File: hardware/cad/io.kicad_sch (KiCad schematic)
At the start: 29 parts, among them J1 DC POWER JACK, J2 1/4" JACK, STEREO, J23 2P_HEADER, J24 2P_HEADER, J25 2P_HEADER, J26 2P_HEADER, J3 6-440054-2, J4 6-440129-2, J5 1/4" JACK, STEREO

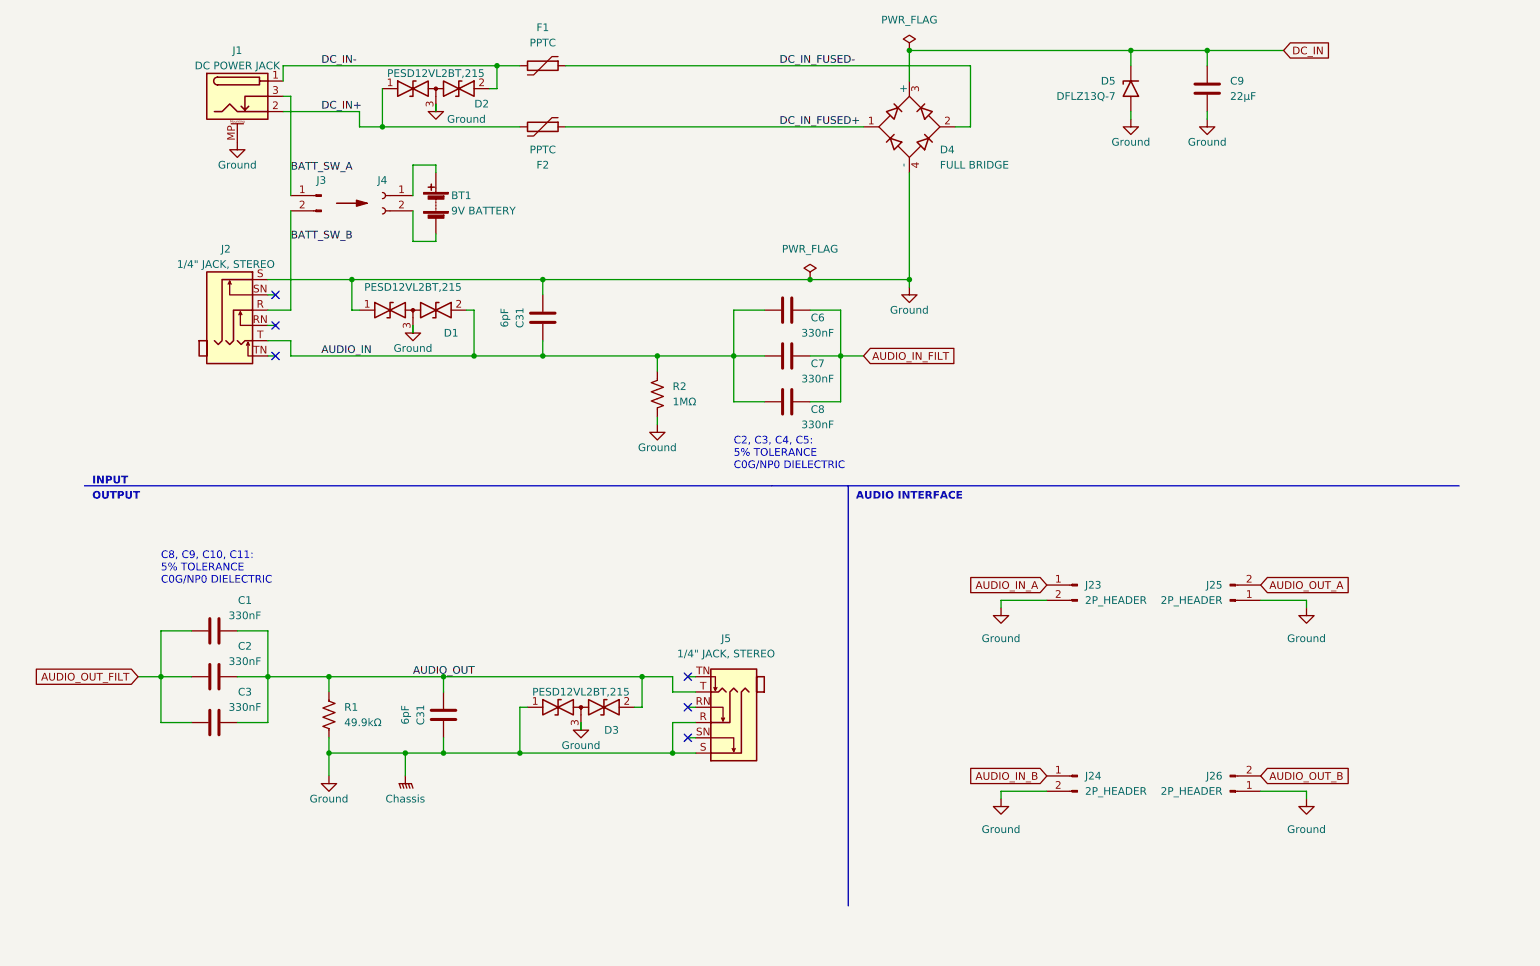
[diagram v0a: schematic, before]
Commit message: added differential inputs and started new layout
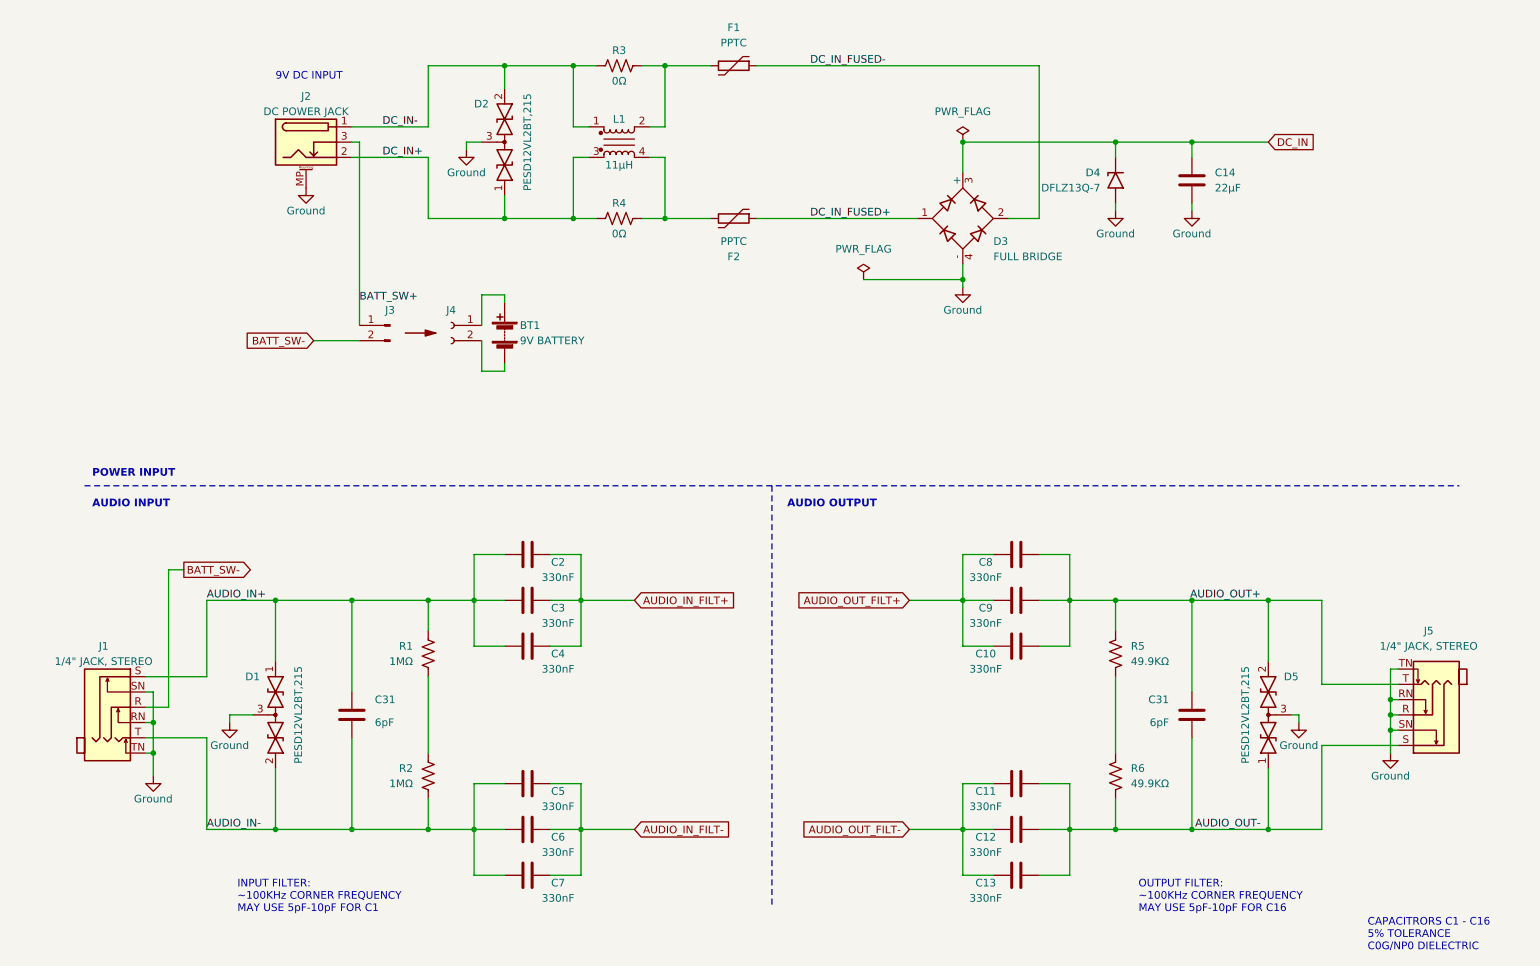
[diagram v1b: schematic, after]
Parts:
- removed C1: 330nF, Capacitor_SMD:C_1206_3216Metric, symbol Device:C
- removed C31 (x2): 6pF, Capacitor_SMD:C_0603_1608Metric, symbol Device:C
- removed CHS1: Chassis, Library:Harwin_EMI_Finger_S7061-46R, symbol Library:Chassis
- removed D3: PESD12VL2BT,215, Package_TO_SOT_SMD:SOT-23, symbol Library:PESD12VL2BT,215
- removed D4: FULL BRIDGE, Package_TO_SOT_SMD:TO-269AA, symbol Library:RH06T
- removed D5: DFLZ13Q-7, Diode_SMD:D_PowerDI-123, symbol Library:DFLZ13Q-7
- removed J1: DC POWER JACK, Library:CUI_PJ-047, symbol Library:DC_POWER_JACK
- removed J2: 1/4" JACK, STEREO, Library:Amphenol_ACJS-IHS, symbol Library:ACJS-IHS
- removed J23, J24, J25, J26: 2P_HEADER, Connector_PinSocket_2.54mm:PinSocket_1x02_P2.54mm_Vertical, symbol Connector:Conn_01x02_Male
- added C10, C11, C12, C13, C4, C5: 330nF, Capacitor_SMD:C_1206_3216Metric, symbol Device:C
- added C14: 22μF, Capacitor_SMD:C_0805_2012Metric, symbol Device:C
- added C31 (x2): 6pF, Capacitor_SMD:C_0603_1608Metric, symbol Device:C
- added D3: FULL BRIDGE, Package_TO_SOT_SMD:TO-269AA, symbol Library:RH06T
- added D4: DFLZ13Q-7, Diode_SMD:D_PowerDI-123, symbol Library:DFLZ13Q-7
- added D5: PESD12VL2BT,215, Package_TO_SOT_SMD:SOT-23, symbol Library:PESD12VL2BT,215
- added J1: 1/4" JACK, STEREO, Library:Amphenol_ACJS-IHS, symbol Library:ACJS-IHS
- added J2: DC POWER JACK, Library:CUI_PJ-047, symbol Library:DC_POWER_JACK
- added L1: 11µH, Library:BOURNS_DR331-113BE, symbol Device:L_Iron_Coupled
- added R3, R4: 0Ω, Resistor_SMD:R_0805_2012Metric, symbol Device:R_US
- added R5, R6: 49.9KΩ, Resistor_SMD:R_0603_1608Metric, symbol Device:R_US
- C9: value 22μF -> 330nF; footprint Capacitor_SMD:C_0805_2012Metric -> Capacitor_SMD:C_1206_3216Metric; Part Number GRM21BR61E226ME44L -> GRM31C5C1E334JE01L
- R1: value 49.9kΩ -> 1MΩ; Part Number RN73H1JTTD4992F100 -> RN73H1JTTD1004F100
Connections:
- net DC_IN: now also C14.2, D3.3 (+), D4.1 (K); no longer C9.2
- net DC_IN+: now also J2.2, L1.3, R4.2; no longer F2.2
- net DC_IN-: now also J2.1, L1.1, R3.2; no longer F1.2
- net DC_IN_FUSED+: now also D3.1
- net DC_IN_FUSED-: now also D3.2
- net GND: now also J5.RN, J5.SN, J5.TN, C14.1, D3.4 (-), D4.2 (A), D5.3 (common), J1.RN, J1.SN, J1.TN, J2.MP (MountPin); no longer C9.1, D1.1 (A1), J5.S, R1.1, R2.2
- net AUDIO_IN renamed AUDIO_IN-
- net AUDIO_IN-: now also R2.2, C31.2, C5.1, J1.T; no longer C8.1, R2.1
- net AUDIO_IN_FILT renamed AUDIO_IN_FILT-
- net AUDIO_IN_FILT-: now also C5.2; no longer C8.2
- net AUDIO_OUT renamed AUDIO_IN_FILT+
- net AUDIO_IN_FILT+: now also C4.2; no longer J5.T, R1.2
- net AUDIO_OUT_FILT renamed AUDIO_IN+
- net AUDIO_IN+: now also D1.1 (A1), R1.1, C31.1, C4.1, J1.S
- net BATT_SW_A renamed BATT_SW+
- net BATT_SW+: now also J2.3
- net BATT_SW_B renamed BATT_SW-
- net BATT_SW-: now also J1.R
- new net: F2.2, L1.4, R4.1
- new net: F1.2, L1.2, R3.1
- new net: R5.2, R6.1
- new net: R1.2, R2.1
- new net AUDIO_OUT+: C10.1, C31.1, C8.1, C9.1, D5.2 (A2), J5.T, R5.1
- new net AUDIO_OUT-: C11.1, C12.1, C13.1, C31.2, D5.1 (A1), J5.S, R6.2
- new net AUDIO_OUT_FILT+: C10.2, C8.2, C9.2
- new net AUDIO_OUT_FILT-: C11.2, C12.2, C13.2
- no-connect marks 6 -> 0
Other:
- note added: "9V DC INPUT"
- note added: "AUDIO INPUT"
- note added: "AUDIO OUTPUT"
- note added: "CAPACITRORS C1 - C16 5% TOLERANCE C0G/NP0 DIELECTRIC"
- note added: "INPUT FILTER: ~100KHz CORNER FREQUENCY MAY USE 5pF-10pF FOR C1"
- note added: "OUTPUT FILTER: ~100KHz CORNER FREQUENCY MAY USE 5pF-10pF FOR C16"
- note added: "POWER INPUT"
- note removed: "AUDIO INTERFACE"
- note removed: "C2, C3, C4, C5: 5% TOLERANCE C0G/NP0 DIELECTRIC"
- note removed: "C8, C9, C10, C11: 5% TOLERANCE C0G/NP0 DIELECTRIC"
- note removed: "INPUT"
- note removed: "OUTPUT"

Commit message: more layout updates
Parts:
- added G1: Chassis, Library:Harwin_EMI_Finger_S7061-46R, symbol Library:Chassis
- C10, C11, C12, C13, C2, C3, C4, C5, C6, C7, C8, C9: value 330nF -> 330n
- C14: value 22μF -> 22u
- C31: value 6pF -> 6p
- L1: value 11µH -> 11u
- R1, R2: value 1MΩ -> 1M
- R3, R4: value 0Ω -> 0R
- R5, R6: value 49.9KΩ -> 49.9K
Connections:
- net GND: now also G1.1 (PWR)
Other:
- note removed: "9V DC INPUT"
- moved on the sheet: BT1, C14, D4, J4
